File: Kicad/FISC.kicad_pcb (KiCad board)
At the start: 2 copper layers, 222.2 x 100.3 mm, 58 parts, among them IC1 DS1233-10+, J1 Data Bus Pin Header, J2 Address Bus Pin Header, J3 uSeq Pin Header, SW1 SW_Push, U1 74LS593, U10 AT28C64B, U11 74HCT574, U12 74HCT574, U13 74HCT574, U14 74HCT574, U15 74HCT541, U16 74HCT541, U17 74HCT574, U18 74HCT161, U19 74HCT138, U2 74LS593, U20 74HCT151, U21 74HCT139, U22 74HCT154, U23 M27C322-100F1, U24 UM245R, U25 AT27C1024-70PU, U26 ECS-100AX-035, U3 74HCT138, U4 74HCT240, U5 74LS469, U6 74LS469, U7 74HCT574, U8 74HCT574, U9 CY628128E

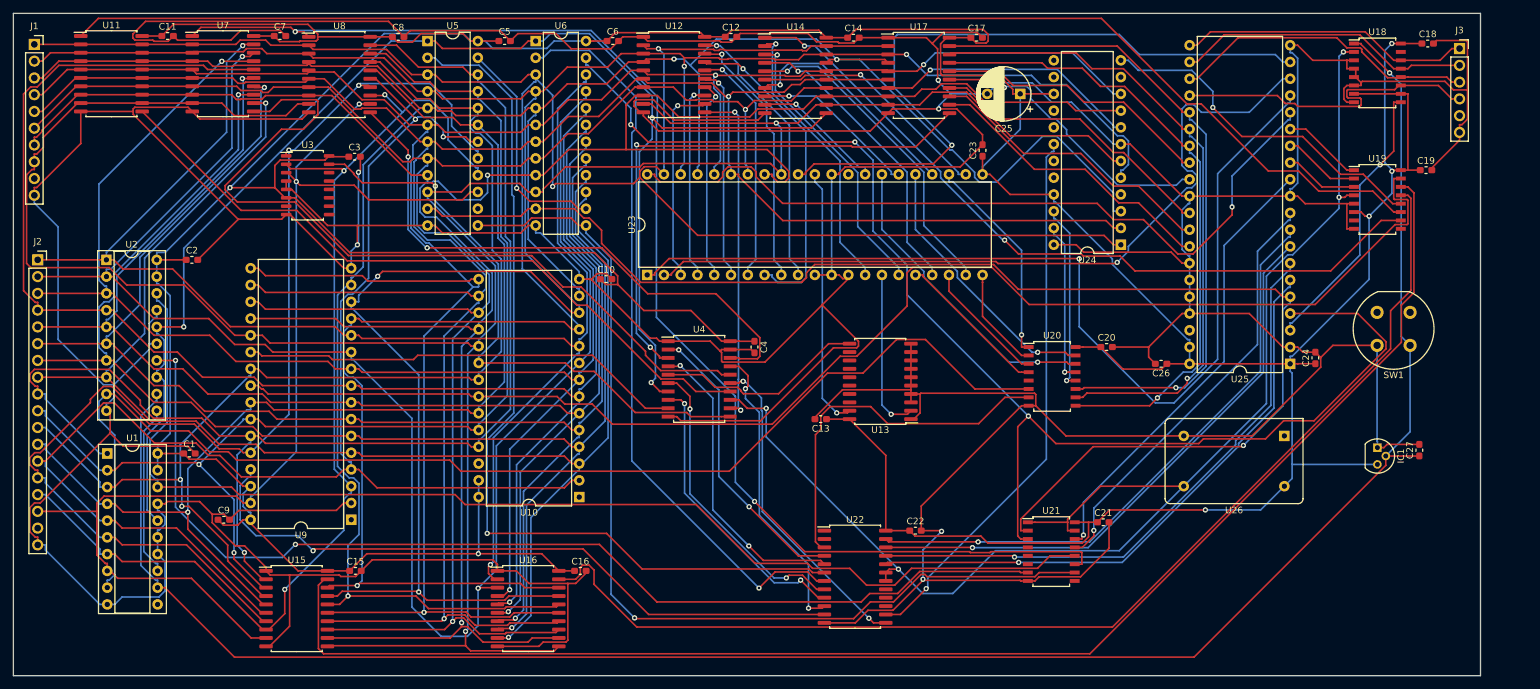
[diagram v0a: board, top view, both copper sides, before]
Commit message: Made a slight update to the PCB layout.
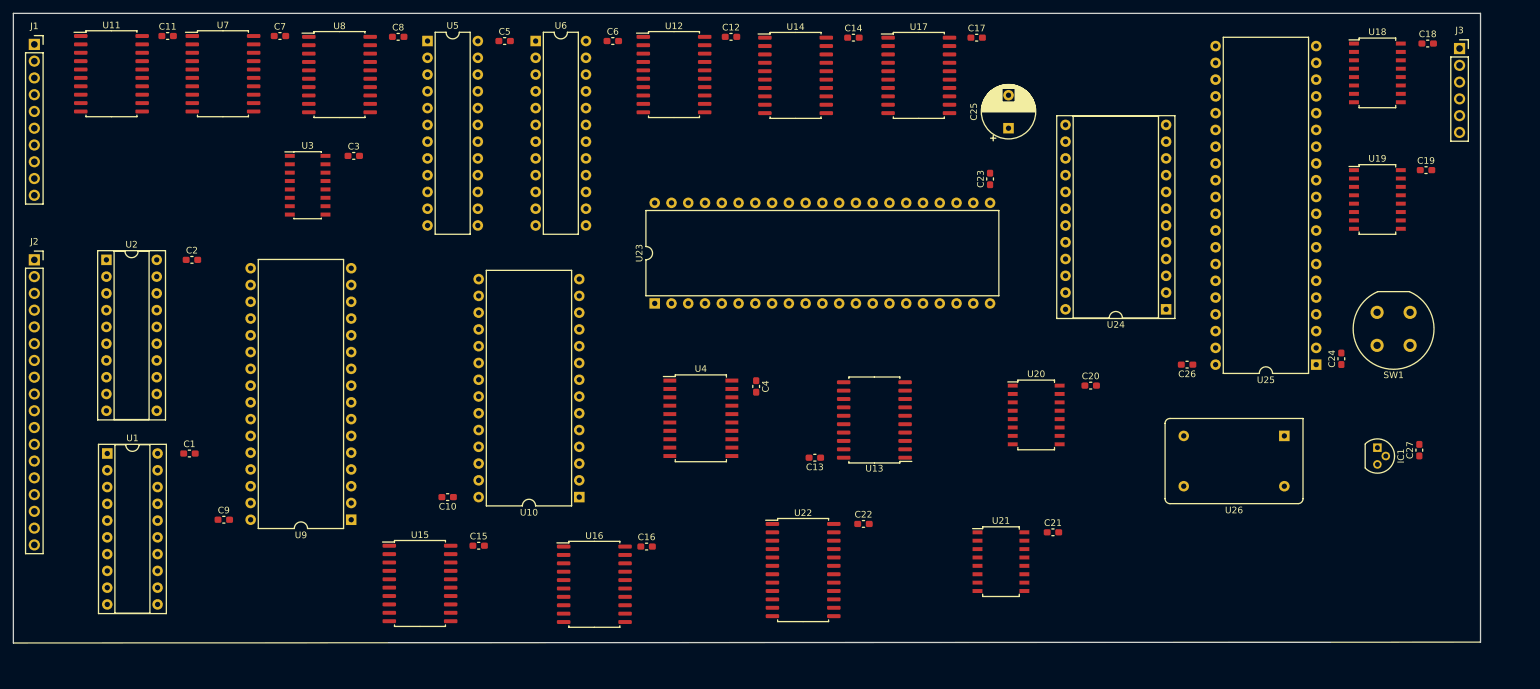
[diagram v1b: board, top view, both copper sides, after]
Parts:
- U24: footprint Package_DIP:DIP-24_W10.16mm -> Package_DIP:DIP-24_W15.24mm_Socket
- U3: footprint Package_SO:SOIC-16_4.55x10.3mm_P1.27mm -> Package_SO:SOIC-16_3.9x9.9mm_P1.27mm
- moved C10 40.8 mm to (84.8, 89.8), turned to 180 degrees
- moved C15 19.1 mm to (89.5, 97.2)
- moved U15 19.1 mm to (80.6, 102.9)
- moved U24 11.9 mm to (193.7, 61.3)
- moved C16 10.7 mm to (115.0, 97.3)
- moved U16 10.7 mm to (107.1, 103.0)
- moved C22 7.94 mm to (147.8, 93.9)
- moved U22 7.94 mm to (138.7, 100.8)
- moved C21 7.77 mm to (176.5, 95.1)
- moved U21 7.77 mm to (168.7, 99.6)
- moved C20 6.32 mm to (182.2, 72.9)
- moved U20 6.32 mm to (174.0, 77.3)
- moved C4 5.97 mm to (131.6, 73.0)
- moved U4 5.97 mm to (123.2, 77.9)
- moved C13 5.91 mm to (140.5, 83.8)
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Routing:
- net Lo: track 1317.3 -> 0.00 mm, vias 6 -> 0
- net Hi: track 797.0 -> 0.00 mm, vias 6 -> 0
- net d0: track 407.2 -> 0.00 mm, vias 3 -> 0
- net d7: track 394.7 -> 0.00 mm, vias 2 -> 0
- net d2: track 373.2 -> 0.00 mm, vias 3 -> 0
- net d6: track 373.0 -> 0.00 mm, vias 2 -> 0
- net d4: track 371.9 -> 0.00 mm, vias 2 -> 0
- net d1: track 364.9 -> 0.00 mm, vias 4 -> 0
- net d3: track 350.4 -> 0.00 mm, vias 3 -> 0
- net d5: track 348.1 -> 0.00 mm, vias 3 -> 0
- net ~Reset: track 308.8 -> 0.00 mm, vias 1 -> 0
- net adr1: track 246.3 -> 0.00 mm, vias 2 -> 0
- net adr3: track 241.6 -> 0.00 mm, vias 1 -> 0
- net ~ADhiwrite: track 221.0 -> 0.00 mm
- net adr2: track 220.0 -> 0.00 mm, vias 2 -> 0
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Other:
- board size 222.2 x 100.3 mm -> 222.2 x 95.4 mm

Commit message: Redid the track layout.
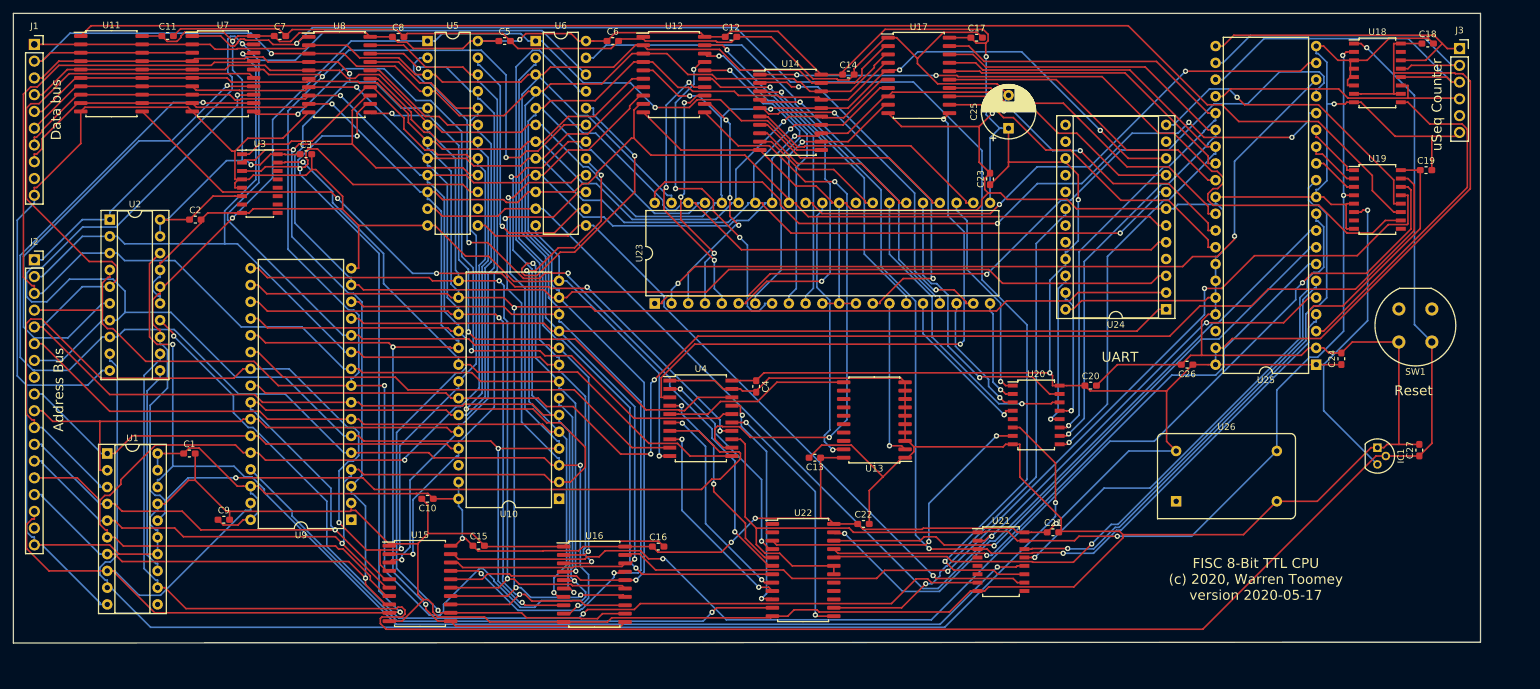
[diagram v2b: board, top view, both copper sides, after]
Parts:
- moved U26 19.1 mm to (195.2, 90.4), turned to 0 degrees
- moved U3 7.24 mm to (56.4, 42.3)
- moved C3 7.24 mm to (63.4, 37.8)
- moved C2 6.12 mm to (46.6, 47.8)
- moved U2 6.12 mm to (33.7, 47.8)
- moved C14 5.64 mm to (145.5, 25.8)
- moved U14 5.64 mm to (136.8, 31.5)
- moved SW1 3.34 mm to (233.9, 66.3)
- moved C10 3.06 mm to (81.8, 90.0)
- moved U10 3.06 mm to (101.7, 90.0)
- moved C16 1.76 mm to (116.7, 97.3)
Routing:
- net Lo: track 0.00 -> 1243.8 mm, vias 0 -> 3
- net Hi: track 0.00 -> 788.6 mm, vias 0 -> 11
- net d2: track 0.00 -> 433.3 mm, vias 0 -> 2
- net d1: track 0.00 -> 426.3 mm, vias 0 -> 3
- net d4: track 0.00 -> 413.0 mm, vias 0 -> 4
- net d0: track 0.00 -> 404.8 mm, vias 0 -> 1
- net d5: track 0.00 -> 378.0 mm, vias 0 -> 5
- net d6: track 0.00 -> 362.0 mm, vias 0 -> 3
- net d3: track 0.00 -> 361.9 mm, vias 0 -> 6
- net d7: track 0.00 -> 356.7 mm, vias 0 -> 4
- net ~Reset: track 0.00 -> 319.6 mm, vias 0 -> 1
- net adr3: track 0.00 -> 290.6 mm, vias 0 -> 4
- net ~Clkbar: track 0.00 -> 274.3 mm, vias 0 -> 3
- net adr4: track 0.00 -> 254.4 mm, vias 0 -> 2
- net adr2: track 0.00 -> 251.0 mm, vias 0 -> 3
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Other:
- board text added: "Address Bus"
- board text added: "Data bus"
- board text added: "FISC 8-Bit TTL CPU (c) 2020, Warren Toomey version 2020-05-17"
- board text added: "Reset"
- board text added: "UART"
- board text added: "uSeq Counter"

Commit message: Added the equ pseudo-op. Rearranged the PCB layout.
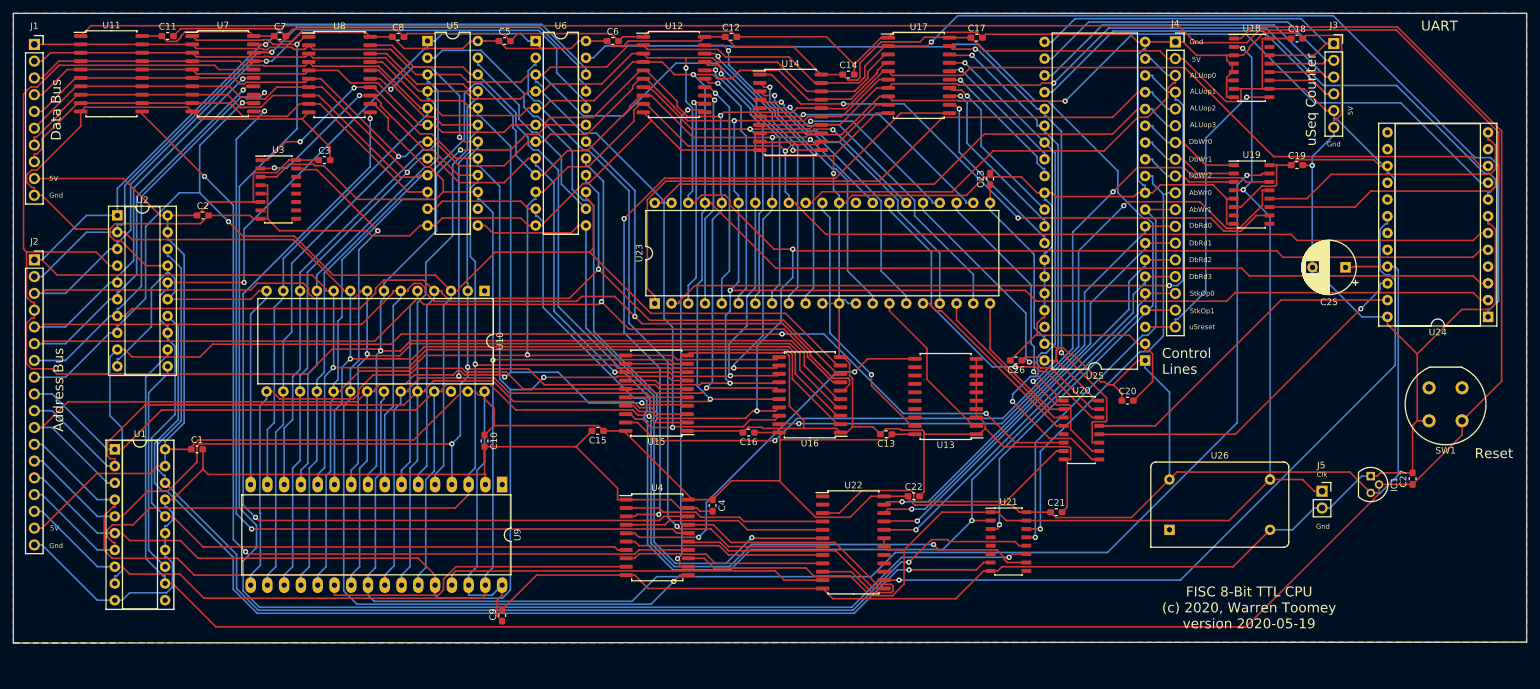
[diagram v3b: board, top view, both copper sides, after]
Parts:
- removed C24: 0.1uF, Capacitor_SMD:C_0603_1608Metric_Pad1.05x0.95mm_HandSolder
- added J4: Control Lines Pin Header, Connector_PinSocket_2.54mm:PinSocket_1x18_P2.54mm_Vertical, F.Cu at (195.1, 20.8)
- added J5: Clock Pin Header, Connector_PinSocket_2.54mm:PinSocket_1x02_P2.54mm_Vertical, F.Cu at (217.3, 88.9)
- U18, U19, U20, U21: footprint Package_SO:SOIC-16W_5.3x10.2mm_P1.27mm -> Package_SO:SOIC-16_3.9x9.9mm_P1.27mm
- U9: value CY628128E -> AS6C1008; footprint Package_DIP:DIP-32_W15.24mm -> Package_DIP:DIP-32_W15.24mm_LongPads
- moved C25 55.2 mm to (220.9, 55.0), turned to 180 degrees
- moved U24 48.8 mm to (242.4, 62.5)
- moved U15 46.0 mm to (116.5, 74.0), turned to 180 degrees
- moved C9 44.6 mm to (93.1, 107.7), turned to 90 degrees
- moved U16 43.5 mm to (139.7, 74.3), turned to 180 degrees
- moved U10 33.5 mm to (90.4, 58.5), turned to 270 degrees
- moved C26 25.9 mm to (170.9, 69.1)
- moved U25 25.9 mm to (190.5, 69.1)
- moved C15 25.1 mm to (107.6, 79.8), turned to 180 degrees
- moved U9 23.5 mm to (93.1, 87.9), turned to 270 degrees
- moved C16 22.0 mm to (130.4, 80.0), turned to 180 degrees
- moved C18 19.8 mm to (213.5, 20.3)
- moved C19 19.6 mm to (213.5, 39.5)
- moved U4 19.2 mm to (116.6, 95.9)
- moved C4 19.2 mm to (125.0, 91.1)
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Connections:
- J1 pad 9: (no net) -> Hi
- J2 pad 17: (no net) -> Hi
- J3 pad 5: (no net) -> Hi
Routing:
- net d7: track 356.7 -> 419.1 mm, vias 4 -> 2
- net ~ADhiwrite: track 183.7 -> 127.0 mm
- net ~Awrite: track 213.6 -> 267.6 mm
- net adr8: track 171.4 -> 220.6 mm
- net ~ADlowrite: track 150.3 -> 102.1 mm
- net ARhiread: track 90.0 -> 136.1 mm
- net d6: track 362.0 -> 405.8 mm
- net adr1: track 222.5 -> 262.3 mm
- net adr9: track 173.6 -> 212.4 mm, vias 2 -> 0
- net d3: track 361.9 -> 398.5 mm, vias 6 -> 2
- net adr0: track 232.6 -> 269.0 mm
- net RAMena: track 91.6 -> 127.9 mm, vias 1 -> 2
- net d5: track 378.0 -> 413.3 mm
- net ~UARTread: track 81.8 -> 115.5 mm
- net DbRd3: track 95.3 -> 62.3 mm
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- added copper zone on B.Cu, net Lo
- added copper zone on F.Cu, net Lo
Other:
- board size 222.2 x 95.4 mm -> 229.2 x 95.4 mm
- board text added: "5V"
- board text added: "ALUop0"
- board text added: "ALUop1"
- board text added: "ALUop2"
- board text added: "ALUop3"
- board text added: "AbWr0"
- board text added: "AbWr1"
- board text added: "Clk"
- board text added: "Control Lines"
- board text added: "Data Bus"
- board text added: "DbRd0"
- board text added: "DbRd1"
- board text added: "DbRd2"
- board text added: "DbRd3"
- board text added: "DbWr0"
- board text added: "DbWr1"
- board text added: "DbWr2"
- board text added: "FISC 8-Bit TTL CPU (c) 2020, Warren Toomey version 2020-05-19"
- board text added: "Gnd"
- board text added: "StkOp0"
- board text added: "StkOp1"
- board text added: "uSreset"
- board text removed: "Data bus"
- board text removed: "FISC 8-Bit TTL CPU (c) 2020, Warren Toomey version 2020-05-17"

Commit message: Updated the schematic. Added some more labels to the PCB silk screen.
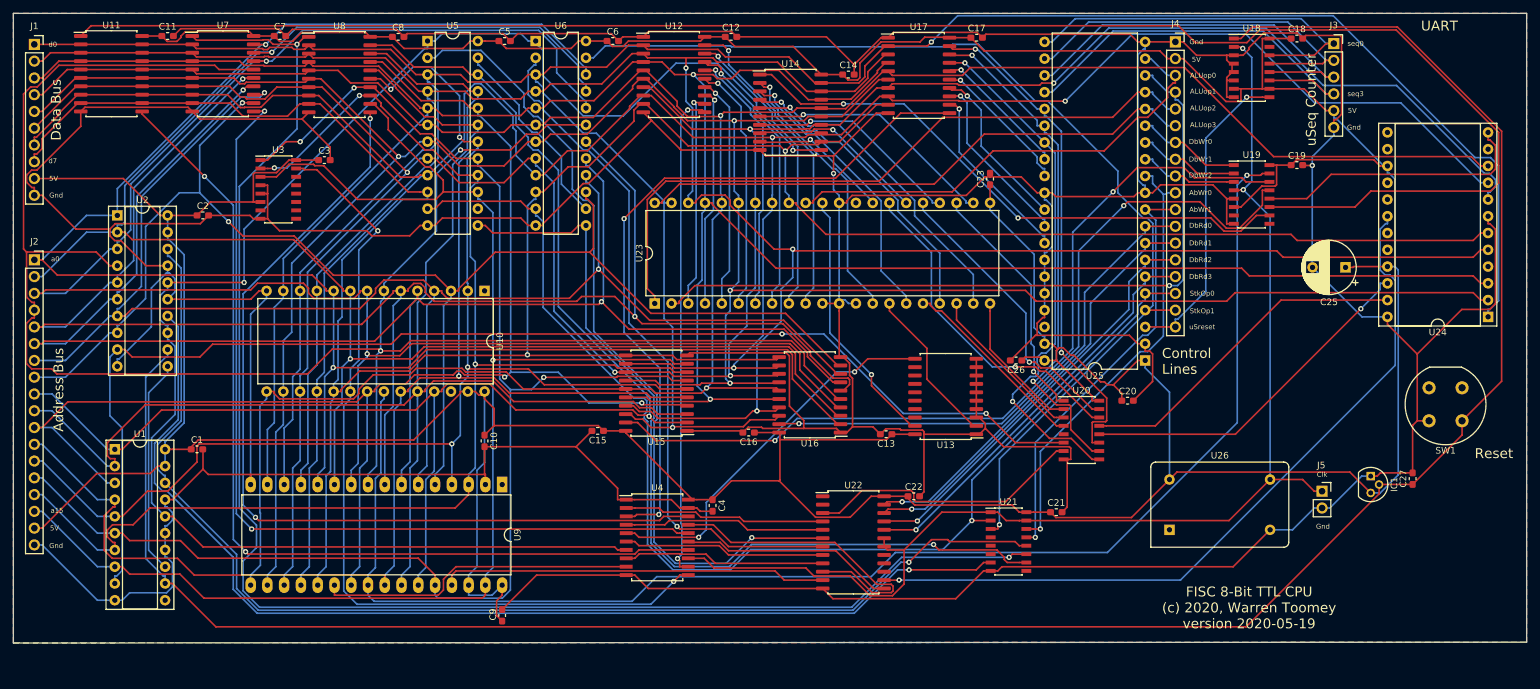
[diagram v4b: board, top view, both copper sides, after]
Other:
- board text added: "a0"
- board text added: "a15"
- board text added: "d0"
- board text added: "d7"
- board text added: "seq0"
- board text added: "seq3"
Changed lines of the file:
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@@
   (general
     (thickness 1.6)
-    (drawings 37)
+    (drawings 43)
     (tracks 3010)
     (zones 0)
@@
     )
   )
+  (gr_text seq3 (at 222.377 28.702) (layer F.SilkS)
+    (effects (font (size 0.75 0.75) (thickness 0.15)))
+  )
+  (gr_text seq0 (at 222.377 21.082) (layer F.SilkS)
+    (effects (font (size 0.75 0.75) (thickness 0.15)))
+  )
+  (gr_text a15 (at 25.654 91.821) (layer F.SilkS)
+    (effects (font (size 0.75 0.75) (thickness 0.15)))
+  )
+  (gr_text a0 (at 25.4 53.721) (layer F.SilkS)
+    (effects (font (size 0.75 0.75) (thickness 0.15)))
+  )
+  (gr_text d7 (at 25.019 38.862) (layer F.SilkS)
+    (effects (font (size 0.75 0.75) (thickness 0.15)))
+  )
+  (gr_text d0 (at 25.019 21.209) (layer F.SilkS)
+    (effects (font (size 0.75 0.75) (thickness 0.15)))
+  )
   (gr_text 5V (at 25.273 94.488) (layer F.SilkS)
     (effects (font (size 0.75 0.75) (thickness 0.15)))
@@
     (effects (font (size 0.75 0.75) (thickness 0.15)))
   )
-  (gr_text 5V (at 221.615 31.242 90) (layer F.SilkS)
+  (gr_text 5V (at 221.869 31.242) (layer F.SilkS)
     (effects (font (size 0.75 0.75) (thickness 0.15)))
   )
@@
     (effects (font (size 0.75 0.75) (thickness 0.15)))
   )
-  (gr_text Gnd (at 219.075 36.322) (layer F.SilkS)
+  (gr_text Gnd (at 222.123 33.782) (layer F.SilkS)
     (effects (font (size 0.75 0.75) (thickness 0.15)))
   )
